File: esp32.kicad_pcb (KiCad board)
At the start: 2 copper layers, 44 x 80.5 mm, 101 parts, among them J1 USB_C, J15 SPI_0, J16 SPI_1, J3 A0, J4 A1, J5 A2, J6 D0, J7 D1, J8 USB_VOUT, Q10 AO3400A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

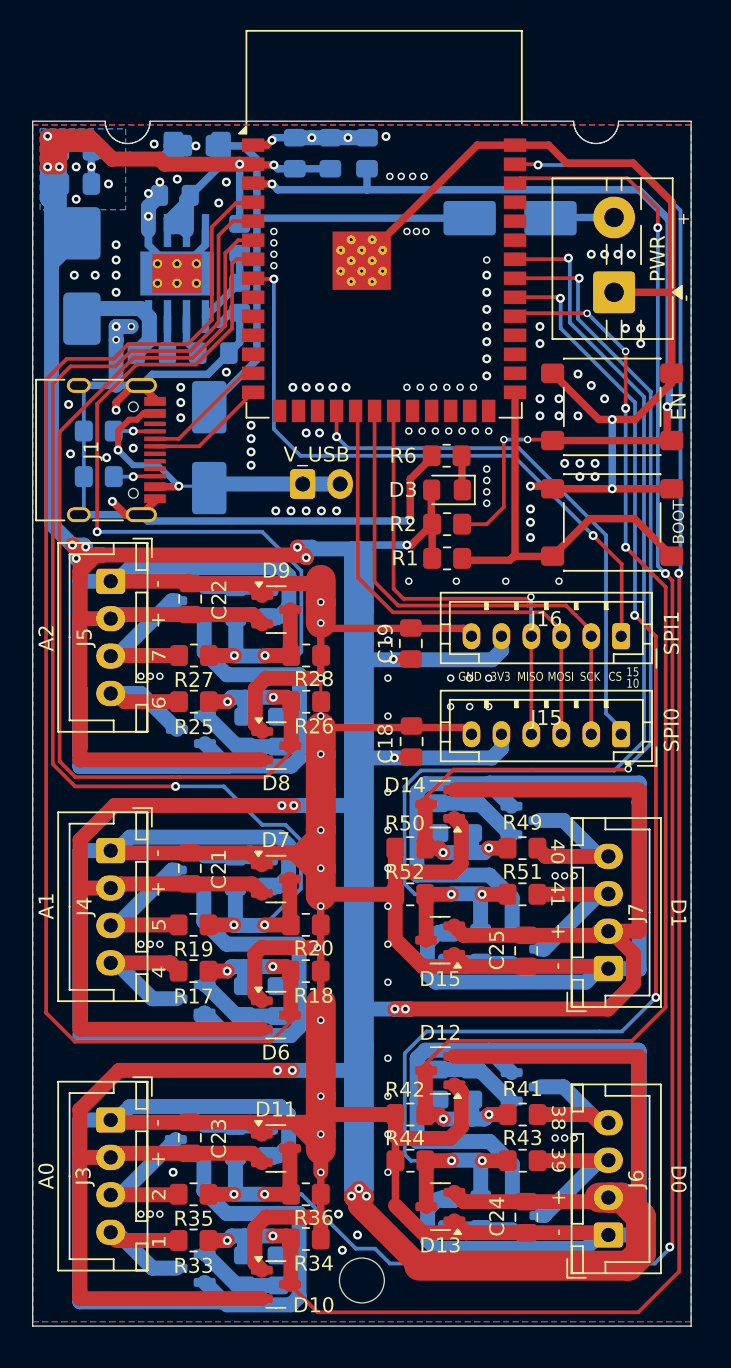
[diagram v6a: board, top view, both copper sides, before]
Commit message: move bottom to align center
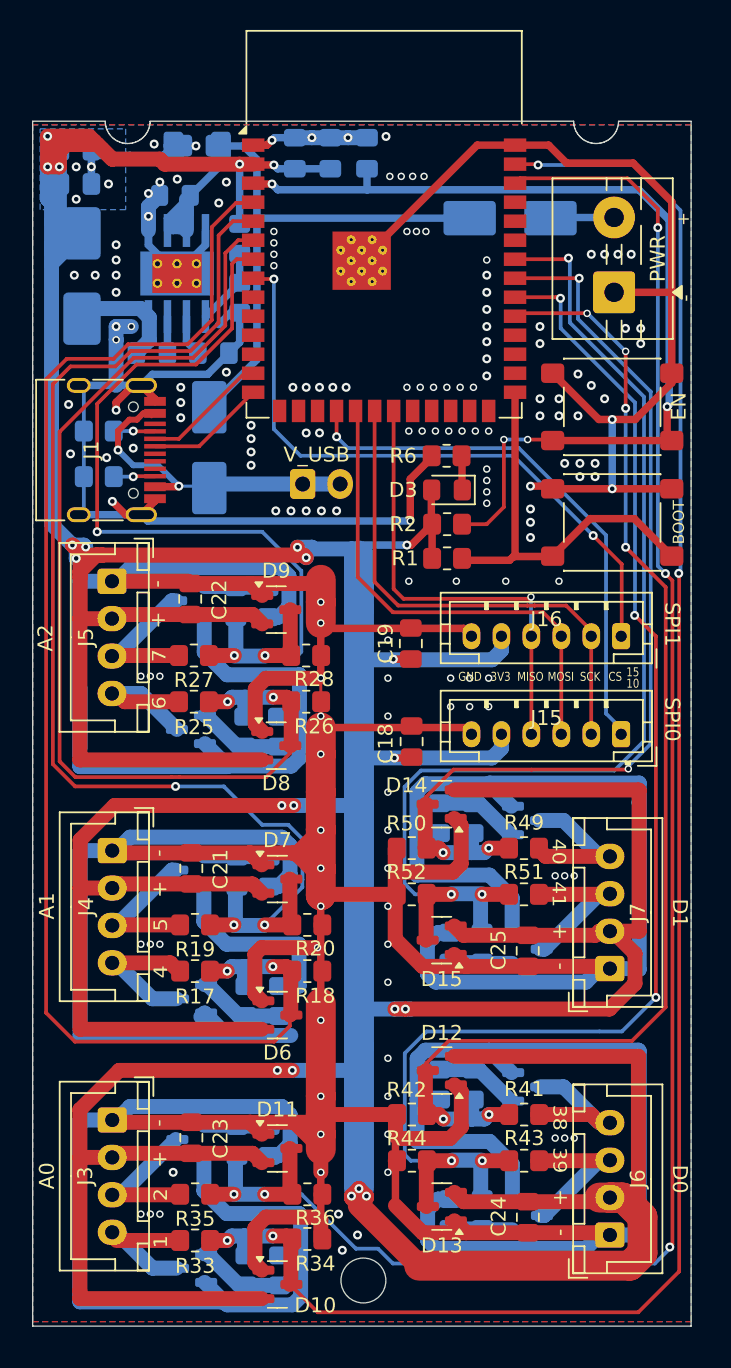
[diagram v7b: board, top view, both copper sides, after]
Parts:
- moved J6 0.10 mm to (109.4, 145.2)
- moved J7 0.10 mm to (109.4, 127.4)
- moved Q3 0.10 mm to (81.5, 129.4)
- moved Q7 0.10 mm to (81.5, 147.4)
- moved Q9 0.10 mm to (103.9, 135.3)
- moved R13 0.10 mm to (87.4, 129.5)
- moved R14 0.10 mm to (86.7, 120.9)
- moved R15 0.10 mm to (85.1, 129.5)
- moved R16 0.10 mm to (84.5, 120.9)
- moved R29 0.10 mm to (87.4, 147.5)
- moved R31 0.10 mm to (85.1, 147.5)
- moved R32 0.10 mm to (84.5, 138.9)
- moved R37 0.10 mm to (98.1, 135.1)
- moved R39 0.10 mm to (100.3, 135.1)
- moved R40 0.10 mm to (100.9, 143.8)
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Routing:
- net GND: track 690.4 -> 687.4 mm
- net +3V3: track 466.9 -> 468.2 mm
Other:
- outline, holes or cut-outs redrawn
